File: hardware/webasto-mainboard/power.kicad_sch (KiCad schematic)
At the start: 14 parts

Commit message: v1.0 layout complete
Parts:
- removed D?: D_Schottky, symbol Device:D_Schottky
- removed U?: BD9G341EFJ, Package_SO:HTSOP-8-1EP_3.9x4.9mm_P1.27mm_EP2.4x3.2mm_ThermalVias, symbol Regulator_Switching:BD9G341EFJ
- added D5: ACDBQC0130L-HF, Diode_SMD:D_SOD-923, symbol Device:D_Schottky
- added U6: BD9G341EFJ, Package_SO:HTSOP-8-1EP_3.9x4.9mm_P1.27mm_EP2.4x3.2mm_ThermalVias, symbol Beirdo:BD9G341EFJ
- C10, C12, C9: renamed from C?; footprint (none) -> Capacitor_SMD:C_0805_2012Metric
- C11: renamed from C?; value 100uF Ta -> 100uF Ta 6V; footprint (none) -> Capacitor_Tantalum_SMD:CP_EIA-3216-10_Kemet-I_Pad1.58x1.35mm_HandSolder
- C8: renamed from C?; footprint (none) -> Capacitor_SMD:C_1210_3225Metric_Pad1.33x2.70mm_HandSolder
- L1: renamed from L?; value 33uH -> 33uH 5A 88mOhm; footprint (none) -> UltraLibrarian:PM4346.333NLT; Digikey (none) -> 553-PM4346.333NLTTR-ND
- R25, R26, R27, R28: renamed from R?; footprint (none) -> Resistor_SMD:R_0805_2012Metric_Pad1.20x1.40mm_HandSolder
- R29: renamed from R?; value 1k3 -> 3.0k; footprint (none) -> Resistor_SMD:R_0805_2012Metric_Pad1.20x1.40mm_HandSolder
- R30: renamed from R?; value 560R -> 750R; footprint (none) -> Resistor_SMD:R_0805_2012Metric_Pad1.20x1.40mm_HandSolder
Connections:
- net +3V3 is gone; now on net +5V: C11.1, C12.1
- net +12V: now also U6.8 (VCC)
- net GND: now also D5.2 (A), U6.2 (GND), U6.9 (GND)
- net at C9.2, L1.1: now also D5.1 (K), U6.1 (LX)
- net +5V: now reaches L1.2, R29.1
- net at R25.2, R26.1: now also U6.6 (EN)
- net at R27.1: now also U6.5 (RT)
- net at R29.2, R30.1: now also U6.4 (FB)
- net at C9.1: now also U6.7 (BST)
- net at C10.1: now also U6.3 (VC)
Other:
- note added: "5V @ 3A"
- note removed: "3.3V @ 3A"
- moved on the sheet: R29, R30

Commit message: Added title block info
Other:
- title: (none) -> Webasto Thermo Top C Replacement Controller
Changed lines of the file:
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@@
 (kicad_sch (version 20211123) (generator eeschema)
   (paper "A4")
+  (title_block
+    (title "Webasto Thermo Top C Replacement Controller")
+    (date "2023-01-19")
+    (rev "v1.0")
+  )
   (junction (at 210.947 59.182) (diameter 0) (color 0 0 0 0)
   )

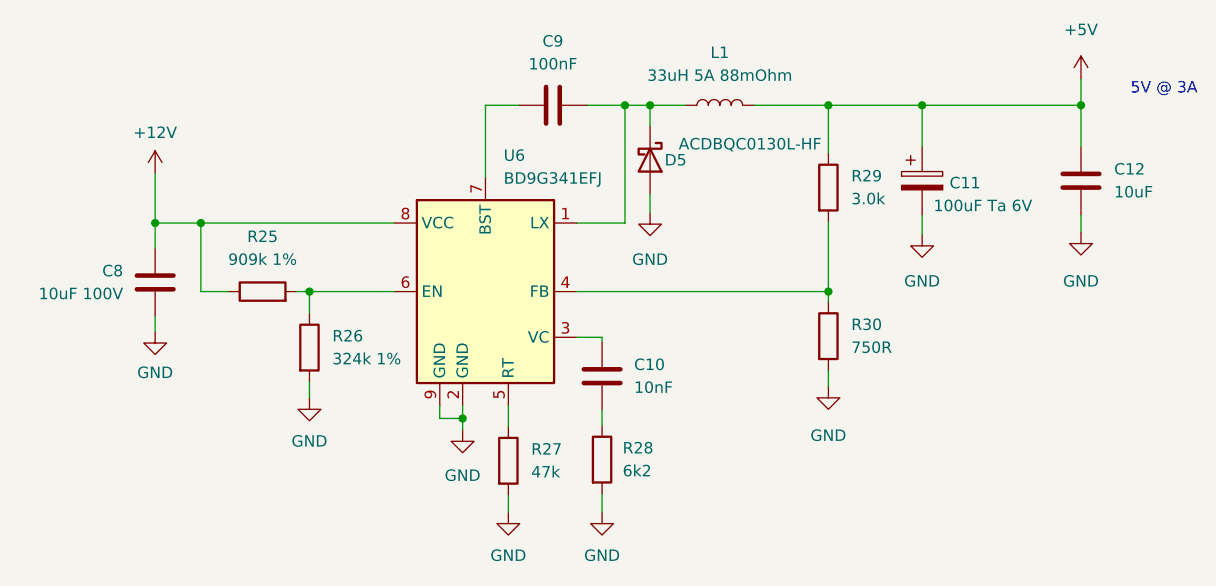
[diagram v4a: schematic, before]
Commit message: Added a 4kbit FRAM on the mainboard to hold nonvolatile
- things like burn hours.
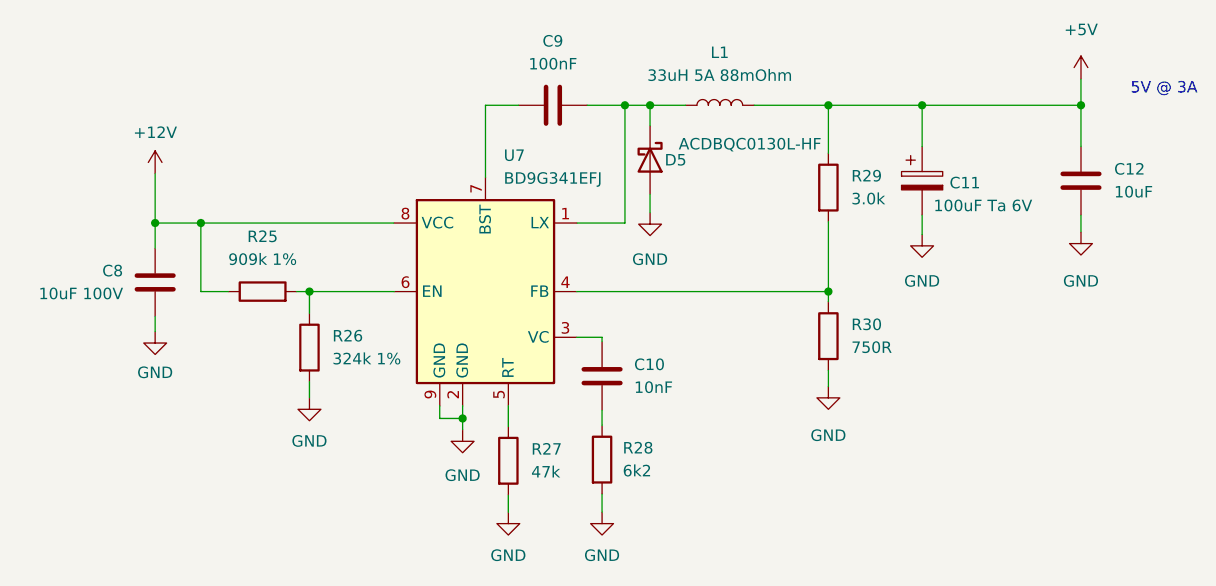
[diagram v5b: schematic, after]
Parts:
- renumbered U6 to U7
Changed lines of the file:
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@@
   (symbol (lib_id "power:GND") (at 210.947 73.279 0) (unit 1)
     (in_bom yes) (on_board yes) (fields_autoplaced)
-    (property "Reference" "#PWR057" (id 0) (at 210.947 79.629 0)
+    (property "Reference" "#PWR061" (id 0) (at 210.947 79.629 0)
       (effects (font (size 1.27 1.27)) hide)
     )
@@
   (symbol (lib_id "power:GND") (at 163.068 71.12 0) (unit 1)
     (in_bom yes) (on_board yes) (fields_autoplaced)
-    (property "Reference" "#PWR053" (id 0) (at 163.068 77.47 0)
+    (property "Reference" "#PWR057" (id 0) (at 163.068 77.47 0)
       (effects (font (size 1.27 1.27)) hide)
     )
@@
   (symbol (lib_id "power:GND") (at 193.294 73.533 0) (unit 1)
     (in_bom yes) (on_board yes) (fields_autoplaced)
-    (property "Reference" "#PWR055" (id 0) (at 193.294 79.883 0)
+    (property "Reference" "#PWR059" (id 0) (at 193.294 79.883 0)
       (effects (font (size 1.27 1.27)) hide)
     )
@@
   (symbol (lib_id "power:GND") (at 108.077 84.328 0) (unit 1)
     (in_bom yes) (on_board yes) (fields_autoplaced)
-    (property "Reference" "#PWR048" (id 0) (at 108.077 90.678 0)
+    (property "Reference" "#PWR052" (id 0) (at 108.077 90.678 0)
       (effects (font (size 1.27 1.27)) hide)
     )
@@
   (symbol (lib_id "power:GND") (at 142.24 95.25 0) (unit 1)
     (in_bom yes) (on_board yes) (fields_autoplaced)
-    (property "Reference" "#PWR050" (id 0) (at 142.24 101.6 0)
+    (property "Reference" "#PWR054" (id 0) (at 142.24 101.6 0)
       (effects (font (size 1.27 1.27)) hide)
     )
@@
   (symbol (lib_id "power:GND") (at 125.222 91.694 0) (unit 1)
     (in_bom yes) (on_board yes) (fields_autoplaced)
-    (property "Reference" "#PWR049" (id 0) (at 125.222 98.044 0)
+    (property "Reference" "#PWR053" (id 0) (at 125.222 98.044 0)
       (effects (font (size 1.27 1.27)) hide)
     )
@@
   (symbol (lib_id "power:+12V") (at 108.077 66.802 0) (unit 1)
     (in_bom yes) (on_board yes) (fields_autoplaced)
-    (property "Reference" "#PWR047" (id 0) (at 108.077 70.612 0)
+    (property "Reference" "#PWR051" (id 0) (at 108.077 70.612 0)
       (effects (font (size 1.27 1.27)) hide)
     )
@@
   (symbol (lib_id "power:GND") (at 182.88 90.424 0) (unit 1)
     (in_bom yes) (on_board yes) (fields_autoplaced)
-    (property "Reference" "#PWR054" (id 0) (at 182.88 96.774 0)
+    (property "Reference" "#PWR058" (id 0) (at 182.88 96.774 0)
       (effects (font (size 1.27 1.27)) hide)
     )
@@
   (symbol (lib_id "power:+5V") (at 210.947 56.261 0) (unit 1)
     (in_bom yes) (on_board yes) (fields_autoplaced)
-    (property "Reference" "#PWR056" (id 0) (at 210.947 60.071 0)
+    (property "Reference" "#PWR060" (id 0) (at 210.947 60.071 0)
       (effects (font (size 1.27 1.27)) hide)
     )
@@
   (symbol (lib_id "Beirdo:BD9G341EFJ") (at 144.78 79.883 0) (unit 1)
     (in_bom yes) (on_board yes) (fields_autoplaced)
-    (property "Reference" "U6" (id 0) (at 146.7994 64.77 0)
+    (property "Reference" "U7" (id 0) (at 146.7994 64.77 0)
       (effects (font (size 1.27 1.27)) (justify left))
     )
@@
   (symbol (lib_id "power:GND") (at 147.32 104.394 0) (unit 1)
     (in_bom yes) (on_board yes) (fields_autoplaced)
-    (property "Reference" "#PWR051" (id 0) (at 147.32 110.744 0)
+    (property "Reference" "#PWR055" (id 0) (at 147.32 110.744 0)
       (effects (font (size 1.27 1.27)) hide)
     )
@@
   (symbol (lib_id "power:GND") (at 157.734 104.394 0) (unit 1)
     (in_bom yes) (on_board yes) (fields_autoplaced)
-    (property "Reference" "#PWR052" (id 0) (at 157.734 110.744 0)
-      (effects (font (size 1.27 1.27)) hide)
-    )
+    (property "Reference" "#PWR056" (id 0) (at 157.734 110.744 0)
+      (effects (font (size 1.27 1.27)) hide)
+    )

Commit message: Added EmergencyStop input.  Hope I never need it.
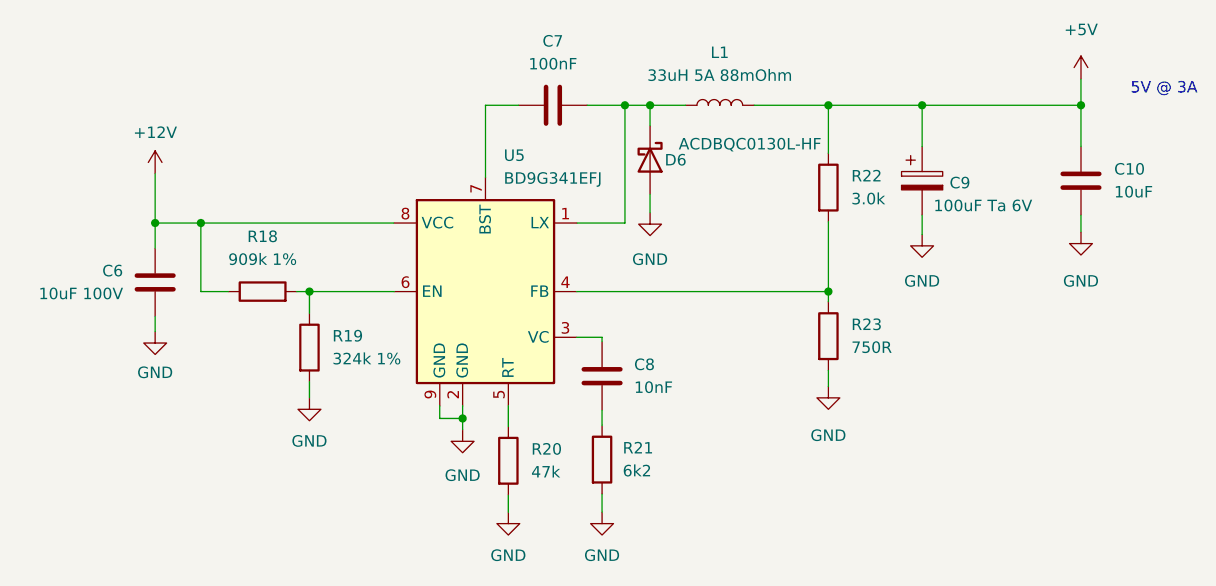
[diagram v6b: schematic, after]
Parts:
- renumbered C12 to C10, C8 to C6, C9 to C7, C10 to C8, C11 to C9, D5 to D6, R25 to R18, R26 to R19, R27 to R20, R28 to R21, R29 to R22, R30 to R23, U7 to U5
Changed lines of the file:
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@@
   (symbol (lib_id "Device:C") (at 210.947 67.564 0) (unit 1)
     (in_bom yes) (on_board yes) (fields_autoplaced)
-    (property "Reference" "C12" (id 0) (at 214.63 66.2939 0)
+    (property "Reference" "C10" (id 0) (at 214.63 66.2939 0)
       (effects (font (size 1.27 1.27)) (justify left))
     )
@@
   (symbol (lib_id "Device:D_Schottky") (at 163.068 65.278 270) (unit 1)
     (in_bom yes) (on_board yes)
-    (property "Reference" "D5" (id 0) (at 167.132 65.278 90)
+    (property "Reference" "D6" (id 0) (at 167.132 65.278 90)
       (effects (font (size 1.27 1.27)) (justify right))
     )
@@
   (symbol (lib_id "Device:R") (at 125.222 86.106 0) (unit 1)
     (in_bom yes) (on_board yes) (fields_autoplaced)
-    (property "Reference" "R26" (id 0) (at 127.762 84.8359 0)
+    (property "Reference" "R19" (id 0) (at 127.762 84.8359 0)
       (effects (font (size 1.27 1.27)) (justify left))
     )
@@
   (symbol (lib_id "power:GND") (at 210.947 73.279 0) (unit 1)
     (in_bom yes) (on_board yes) (fields_autoplaced)
-    (property "Reference" "#PWR061" (id 0) (at 210.947 79.629 0)
+    (property "Reference" "#PWR052" (id 0) (at 210.947 79.629 0)
       (effects (font (size 1.27 1.27)) hide)
     )
@@
   (symbol (lib_id "Device:R") (at 147.32 98.679 0) (unit 1)
     (in_bom yes) (on_board yes) (fields_autoplaced)
-    (property "Reference" "R27" (id 0) (at 149.86 97.4089 0)
+    (property "Reference" "R20" (id 0) (at 149.86 97.4089 0)
       (effects (font (size 1.27 1.27)) (justify left))
     )
@@
   (symbol (lib_id "Device:C") (at 108.077 78.867 0) (mirror y) (unit 1)
     (in_bom yes) (on_board yes)
-    (property "Reference" "C8" (id 0) (at 104.521 77.5969 0)
+    (property "Reference" "C6" (id 0) (at 104.521 77.5969 0)
       (effects (font (size 1.27 1.27)) (justify left))
     )
@@
   (symbol (lib_id "power:GND") (at 163.068 71.12 0) (unit 1)
     (in_bom yes) (on_board yes) (fields_autoplaced)
-    (property "Reference" "#PWR057" (id 0) (at 163.068 77.47 0)
+    (property "Reference" "#PWR048" (id 0) (at 163.068 77.47 0)
       (effects (font (size 1.27 1.27)) hide)
     )
@@
   (symbol (lib_id "Device:R") (at 182.88 68.326 0) (unit 1)
     (in_bom yes) (on_board yes) (fields_autoplaced)
-    (property "Reference" "R29" (id 0) (at 185.42 67.0559 0)
+    (property "Reference" "R22" (id 0) (at 185.42 67.0559 0)
       (effects (font (size 1.27 1.27)) (justify left))
     )
@@
   (symbol (lib_id "power:GND") (at 193.294 73.533 0) (unit 1)
     (in_bom yes) (on_board yes) (fields_autoplaced)
-    (property "Reference" "#PWR059" (id 0) (at 193.294 79.883 0)
+    (property "Reference" "#PWR050" (id 0) (at 193.294 79.883 0)
       (effects (font (size 1.27 1.27)) hide)
     )
@@
   (symbol (lib_id "Device:R") (at 182.88 84.836 0) (unit 1)
     (in_bom yes) (on_board yes) (fields_autoplaced)
-    (property "Reference" "R30" (id 0) (at 185.42 83.5659 0)
+    (property "Reference" "R23" (id 0) (at 185.42 83.5659 0)
       (effects (font (size 1.27 1.27)) (justify left))
     )
@@
   (symbol (lib_id "Device:C") (at 152.273 59.182 90) (unit 1)
     (in_bom yes) (on_board yes) (fields_autoplaced)
-    (property "Reference" "C9" (id 0) (at 152.273 52.07 90))
+    (property "Reference" "C7" (id 0) (at 152.273 52.07 90))
     (property "Value" "100nF" (id 1) (at 152.273 54.61 90))
     (property "Footprint" "Capacitor_SMD:C_0805_2012Metric" (id 2) (at 156.083 58.2168 0)
@@
   (symbol (lib_id "power:GND") (at 108.077 84.328 0) (unit 1)
     (in_bom yes) (on_board yes) (fields_autoplaced)
-    (property "Reference" "#PWR052" (id 0) (at 108.077 90.678 0)
+    (property "Reference" "#PWR043" (id 0) (at 108.077 90.678 0)
       (effects (font (size 1.27 1.27)) hide)
     )
@@
   (symbol (lib_id "power:GND") (at 142.24 95.25 0) (unit 1)
     (in_bom yes) (on_board yes) (fields_autoplaced)
-    (property "Reference" "#PWR054" (id 0) (at 142.24 101.6 0)
+    (property "Reference" "#PWR045" (id 0) (at 142.24 101.6 0)
       (effects (font (size 1.27 1.27)) hide)
     )
@@
   (symbol (lib_id "power:GND") (at 125.222 91.694 0) (unit 1)
     (in_bom yes) (on_board yes) (fields_autoplaced)
-    (property "Reference" "#PWR053" (id 0) (at 125.222 98.044 0)
+    (property "Reference" "#PWR044" (id 0) (at 125.222 98.044 0)
       (effects (font (size 1.27 1.27)) hide)
     )
@@
   (symbol (lib_id "power:+12V") (at 108.077 66.802 0) (unit 1)
     (in_bom yes) (on_board yes) (fields_autoplaced)
-    (property "Reference" "#PWR051" (id 0) (at 108.077 70.612 0)
+    (property "Reference" "#PWR042" (id 0) (at 108.077 70.612 0)
       (effects (font (size 1.27 1.27)) hide)
     )
@@
   (symbol (lib_id "Device:C_Polarized") (at 193.294 67.564 0) (unit 1)
     (in_bom yes) (on_board yes)
-    (property "Reference" "C11" (id 0) (at 196.342 67.818 0)
+    (property "Reference" "C9" (id 0) (at 196.342 67.818 0)
       (effects (font (size 1.27 1.27)) (justify left))
     )
@@
   (symbol (lib_id "power:GND") (at 182.88 90.424 0) (unit 1)
     (in_bom yes) (on_board yes) (fields_autoplaced)
-    (property "Reference" "#PWR058" (id 0) (at 182.88 96.774 0)
+    (property "Reference" "#PWR049" (id 0) (at 182.88 96.774 0)
       (effects (font (size 1.27 1.27)) hide)
     )
@@
   (symbol (lib_id "power:+5V") (at 210.947 56.261 0) (unit 1)
     (in_bom yes) (on_board yes) (fields_autoplaced)
-    (property "Reference" "#PWR060" (id 0) (at 210.947 60.071 0)
+    (property "Reference" "#PWR051" (id 0) (at 210.947 60.071 0)
       (effects (font (size 1.27 1.27)) hide)
     )
@@
   (symbol (lib_id "Device:R") (at 120.015 79.883 90) (unit 1)
     (in_bom yes) (on_board yes) (fields_autoplaced)
-    (property "Reference" "R25" (id 0) (at 120.015 73.787 90))
+    (property "Reference" "R18" (id 0) (at 120.015 73.787 90))
     (property "Value" "909k 1%" (id 1) (at 120.015 76.327 90))
     (property "Footprint" "Resistor_SMD:R_0805_2012Metric_Pad1.20x1.40mm_HandSolder" (id 2) (at 120.015 81.661 90)
@@
   (symbol (lib_id "Beirdo:BD9G341EFJ") (at 144.78 79.883 0) (unit 1)
     (in_bom yes) (on_board yes) (fields_autoplaced)
-    (property "Reference" "U7" (id 0) (at 146.7994 64.77 0)
+    (property "Reference" "U5" (id 0) (at 146.7994 64.77 0)
       (effects (font (size 1.27 1.27)) (justify left))
     )
@@
   (symbol (lib_id "power:GND") (at 147.32 104.394 0) (unit 1)
     (in_bom yes) (on_board yes) (fields_autoplaced)
-    (property "Reference" "#PWR055" (id 0) (at 147.32 110.744 0)
+    (property "Reference" "#PWR046" (id 0) (at 147.32 110.744 0)
       (effects (font (size 1.27 1.27)) hide)
     )
@@
   (symbol (lib_id "Device:R") (at 157.734 98.552 0) (unit 1)
     (in_bom yes) (on_board yes) (fields_autoplaced)
-    (property "Reference" "R28" (id 0) (at 160.02 97.2819 0)
+    (property "Reference" "R21" (id 0) (at 160.02 97.2819 0)
       (effects (font (size 1.27 1.27)) (justify left))
     )
@@
   (symbol (lib_id "Device:C") (at 157.734 89.281 0) (unit 1)
     (in_bom yes) (on_board yes) (fields_autoplaced)
-    (property "Reference" "C10" (id 0) (at 161.29 88.0109 0)
+    (property "Reference" "C8" (id 0) (at 161.29 88.0109 0)
       (effects (font (size 1.27 1.27)) (justify left))
     )
@@
   (symbol (lib_id "power:GND") (at 157.734 104.394 0) (unit 1)
     (in_bom yes) (on_board yes) (fields_autoplaced)
-    (property "Reference" "#PWR056" (id 0) (at 157.734 110.744 0)
-      (effects (font (size 1.27 1.27)) hide)
-    )
+    (property "Reference" "#PWR047" (id 0) (at 157.734 110.744 0)
+      (effects (font (size 1.27 1.27)) hide)
+    )
